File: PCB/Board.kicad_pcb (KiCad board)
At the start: 2 copper layers, 90.5 x 66.7 mm, 12 parts, among them SW1 SW_Push, SW2 SW_Push, SW3 SW_Push, SW4 SW_Push, SW5 SW_Push, SW6 SW_Push, SW7 SW_Push, SW8 SW_Push, SW9 SW_Push, U1 XIAO-RP2040-DIP

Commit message: Update Board.kicad_pcb
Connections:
- SW1 pad 1: Net-(U1-GPIO1/RX) -> Net-(U1-GPIO0/TX)
- SW1 pad 2: unconnected-(SW1-Pad2) -> GND
- SW2 pad 1: unconnected-(SW2-Pad1) -> GND
- SW2 pad 2: Net-(U1-GPIO2/SCK) -> Net-(U1-GPIO0/TX)
- SW3 pad 1: unconnected-(SW3-Pad1) -> GND
- SW3 pad 2: Net-(U1-GPIO4/MISO) -> Net-(U1-GPIO0/TX)
- SW4 pad 1: unconnected-(SW4-Pad1) -> GND
- SW4 pad 2: Net-(U1-GPIO3/MOSI) -> Net-(U1-GPIO0/TX)
- SW5 pad 2: unconnected-(SW5-Pad2) -> GND
- SW6 pad 2: unconnected-(SW6-Pad2) -> GND
- SW8 pad 1: unconnected-(SW8-Pad1) -> Net-(U1-GPIO26/ADC0/A0)
- SW8 pad 2: Net-(U1-GPIO26/ADC0/A0) -> GND
- SW9 pad 2: unconnected-(SW9-Pad2) -> GND
- U1 pad 10: Net-(U1-GPIO4/MISO) -> Net-(U1-GPIO0/TX)
- U1 pad 11: Net-(U1-GPIO3/MOSI) -> Net-(U1-GPIO0/TX)
- U1 pad 8: Net-(U1-GPIO1/RX) -> Net-(U1-GPIO0/TX)
- U1 pad 9: Net-(U1-GPIO2/SCK) -> Net-(U1-GPIO0/TX)
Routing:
- net Net-(U1-GPIO0/TX): track 39.8 -> 321.2 mm
- net Net-(U1-GPIO2/SCK): track 81.4 -> 0.00 mm
- net Net-(U1-GPIO4/MISO): track 77.9 -> 0.00 mm
- net Net-(U1-GPIO1/RX): track 64.1 -> 0.00 mm
- net Net-(U1-GPIO3/MOSI): track 58.0 -> 0.00 mm

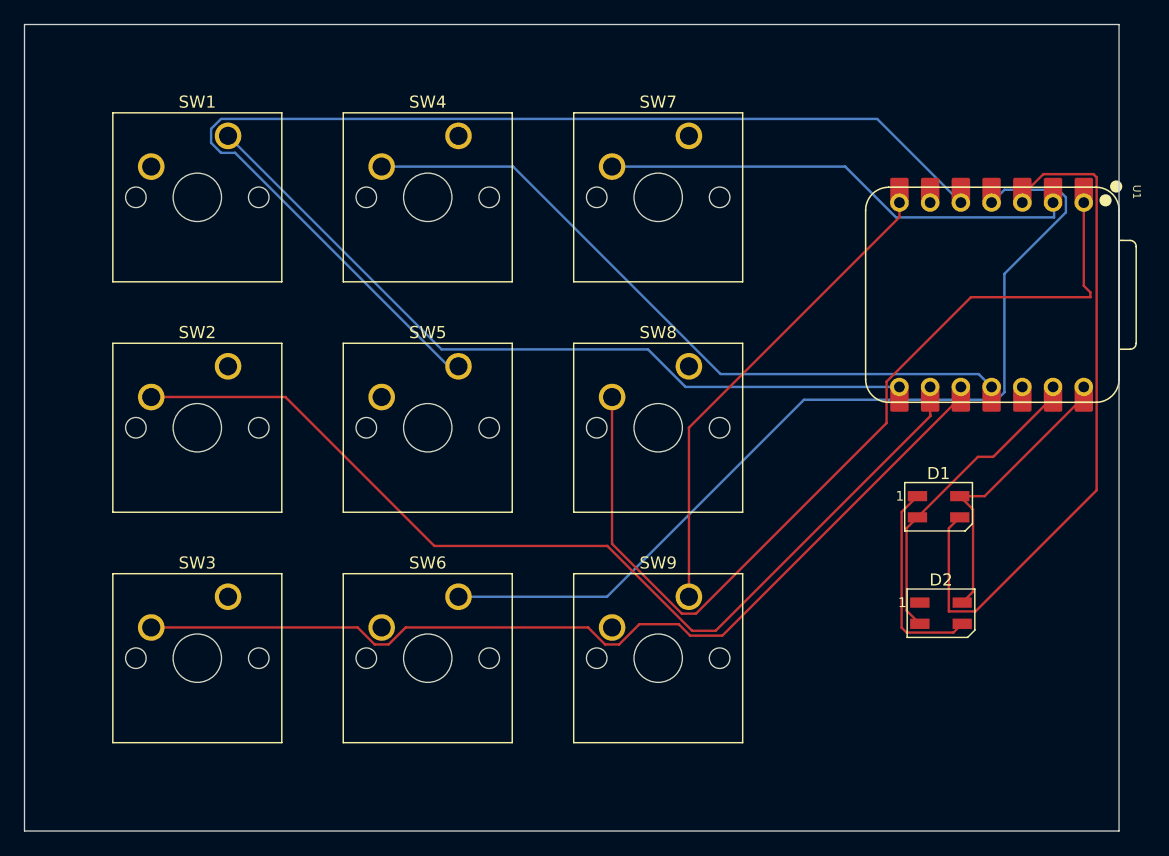
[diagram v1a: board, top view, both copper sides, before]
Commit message: Add labels and clean up PCB segments
Added text labels to the PCB design for better identification and removed several unnecessary segments.
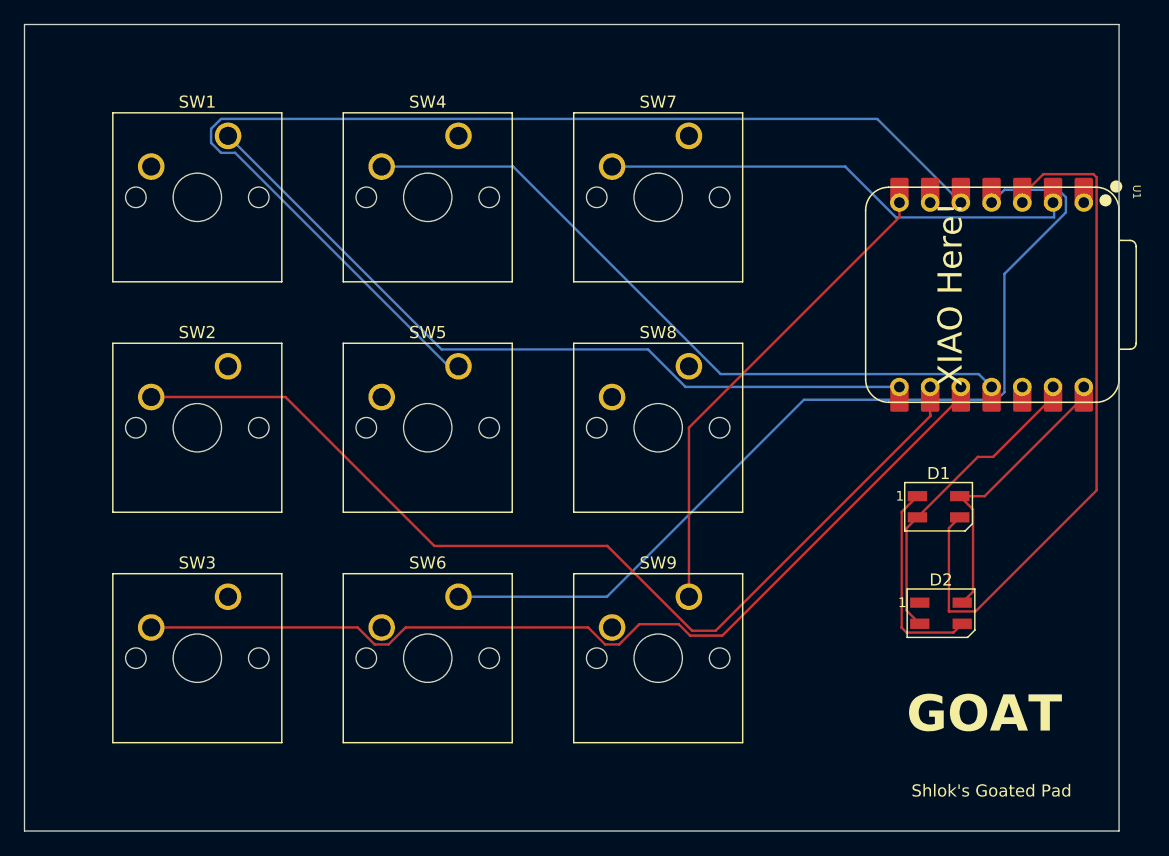
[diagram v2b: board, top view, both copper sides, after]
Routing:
- net Net-(U1-GPIO26/ADC0/A0): track 75.0 -> 0.00 mm
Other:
- board text added: "GOAT"
- board text added: "XIAO Here!"
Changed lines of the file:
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@@
 		(layer "Edge.Cuts")
+	)
+	(gr_text "GOAT"
+		(at 189.6 127.8 0)
+		(layer "F.SilkS")
+		(effects
+			(font
+				(size 3 3)
+				(thickness 0.6)
+				(bold yes)
+			)
+			(justify left bottom)
+		)
+	)
+	(gr_text "Shlok's Goated Pad"
+		(at 190 133 0)
+		(layer "F.SilkS")
+		(effects
+			(font
+				(size 1 1)
+				(thickness 0.1)
+			)
+			(justify left bottom)
+		)
+	)
+	(gr_text "XIAO Here!"
+		(at 194.4 99 90)
+		(layer "F.SilkS")
+		(effects
+			(font
+				(size 2 2)
+				(thickness 0.2)
+			)
+			(justify left bottom)
+		)
 	)
 	(gr_text "Shlok's Goated Pad"
@@
 	)
 	(segment
-		(start 204.2515 90.6515)
-		(end 204.2515 83.78)
-		(width 0.2)
-		(layer "F.Cu")
-		(net 12)
-	)
-	(segment
-		(start 204.8 91.6)
-		(end 204.8 91.2)
-		(width 0.2)
-		(layer "F.Cu")
-		(net 12)
-	)
-	(segment
-		(start 165.25875 111.995064)
-		(end 171.028436 117.76475)
-		(width 0.2)
-		(layer "F.Cu")
-		(net 12)
-	)
-	(segment
-		(start 172.189064 117.76475)
-		(end 187.9485 102.005314)
-		(width 0.2)
-		(layer "F.Cu")
-		(net 12)
-	)
-	(segment
-		(start 165.25875 99.85375)
-		(end 165.25875 111.995064)
-		(width 0.2)
-		(layer "F.Cu")
-		(net 12)
-	)
-	(segment
-		(start 187.9485 98.57969)
-		(end 194.92819 91.6)
-		(width 0.2)
-		(layer "F.Cu")
-		(net 12)
-	)
-	(segment
-		(start 171.028436 117.76475)
-		(end 172.189064 117.76475)
-		(width 0.2)
-		(layer "F.Cu")
-		(net 12)
-	)
-	(segment
-		(start 194.92819 91.6)
-		(end 204.8 91.6)
-		(width 0.2)
-		(layer "F.Cu")
-		(net 12)
-	)
-	(segment
-		(start 204.8 91.2)
-		(end 204.2515 90.6515)
-		(width 0.2)
-		(layer "F.Cu")
-		(net 12)
-	)
-	(segment
-		(start 187.9485 102.005314)
-		(end 187.9485 98.57969)
-		(width 0.2)
-		(layer "F.Cu")
-		(net 12)
-	)
-	(segment
